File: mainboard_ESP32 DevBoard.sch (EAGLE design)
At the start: 44 parts, among them IC1 OP-AMP-2-LONG, IC3 74HC08N, K1 AQH213, X1 JST-XH-02-PIN-LONG-PAD, X2 JST-XH-04-PIN-LONG-PAD, X5 JST-XH-04-PIN-LONG-PAD, X7 1751293

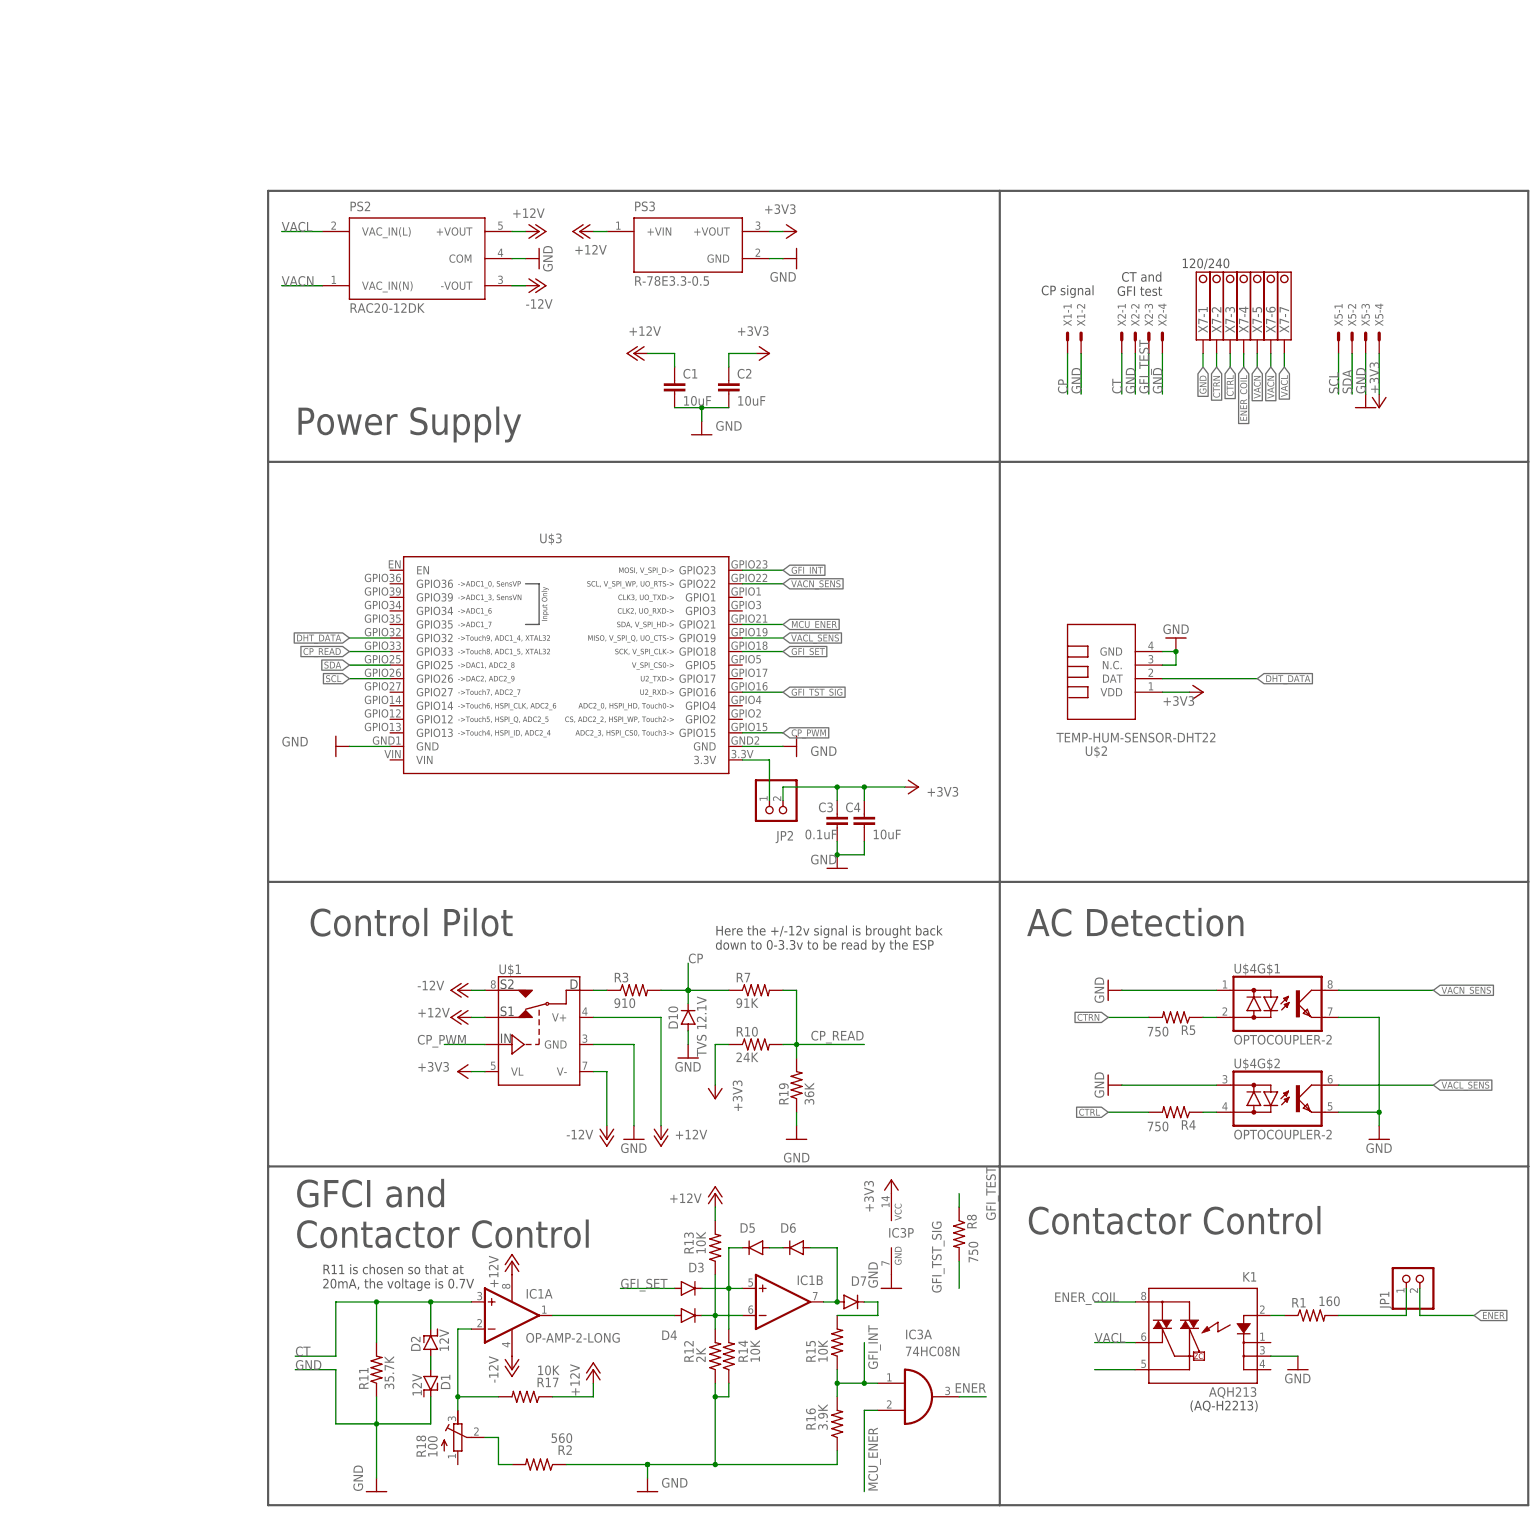
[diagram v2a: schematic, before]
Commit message: Cleaned labels
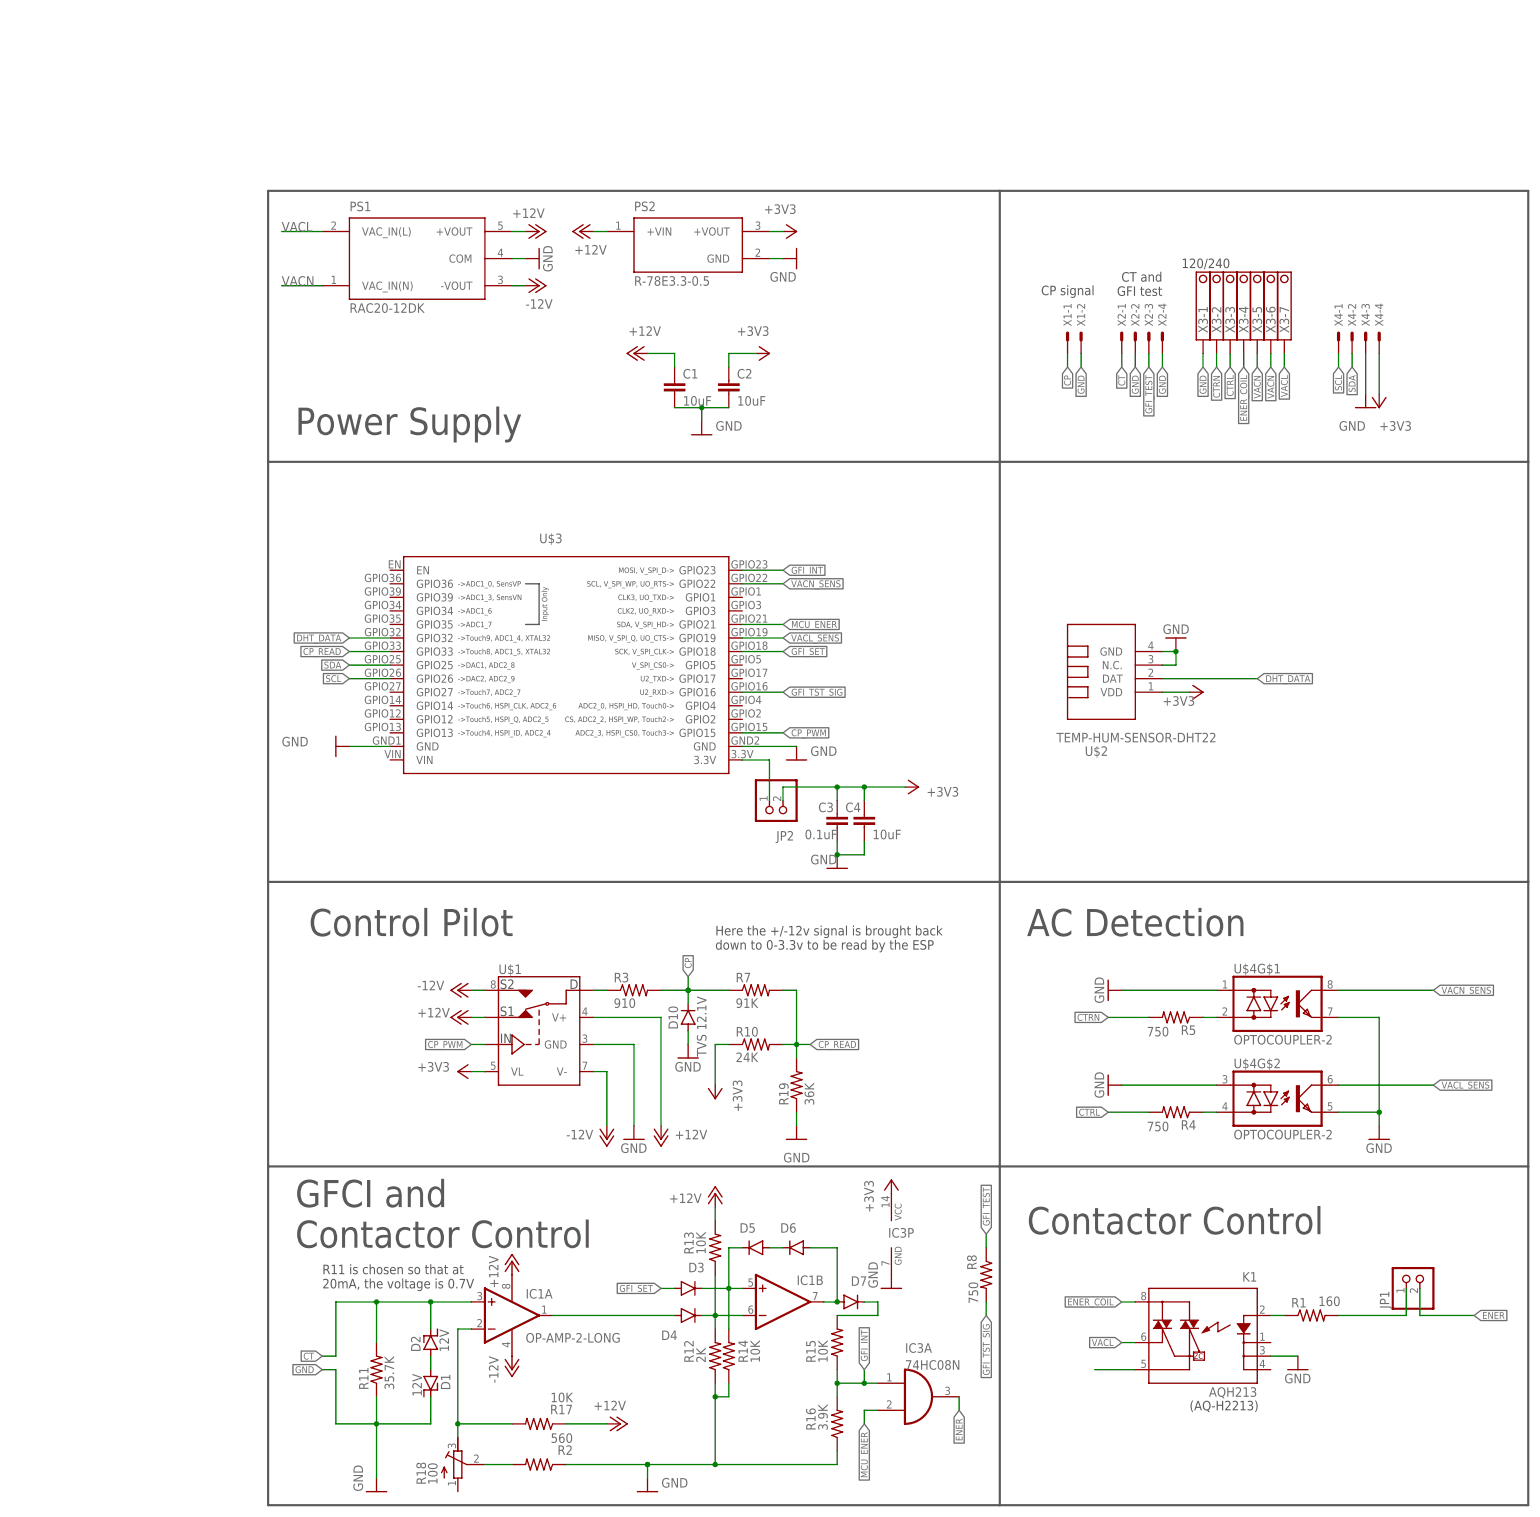
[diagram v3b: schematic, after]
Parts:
- removed PS3: R-78E3.3-0.5, R-78E3.3-0.5:R-78E3.3-0.5
- added PS1: RAC20-12DK, RAC20-12DK:RAC20-12DK
- PS2: value RAC20-12DK -> R-78E3.3-0.5; device RAC20-12DK:RAC20-12DK -> R-78E3.3-0.5:R-78E3.3-0.5
- renumbered X5 to X4, X7 to X3
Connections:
- net +12V: now also PS1.+VOUT, PS2.+VIN; no longer PS2.+VOUT, PS3.+VIN
- net +3V3: now also PS2.+VOUT; no longer PS3.+VOUT
- net -12V: now also PS1.-VOUT; no longer PS2.-VOUT
- net GND: now also PS1.COM, PS2.GND; no longer PS2.COM, PS3.GND
- net VACL: now also PS1.VAC_IN(L); no longer PS2.VAC_IN(L)
- net VACN: now also PS1.VAC_IN(N); no longer PS2.VAC_IN(N)
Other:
- moved on the sheet: R17, R18, R8

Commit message: Reworked GFCI to account for noise on the line. Swapped out AND gate for 2 mosfets. Removed mostly useless caps from PSU outputs, caps should be closer to devices
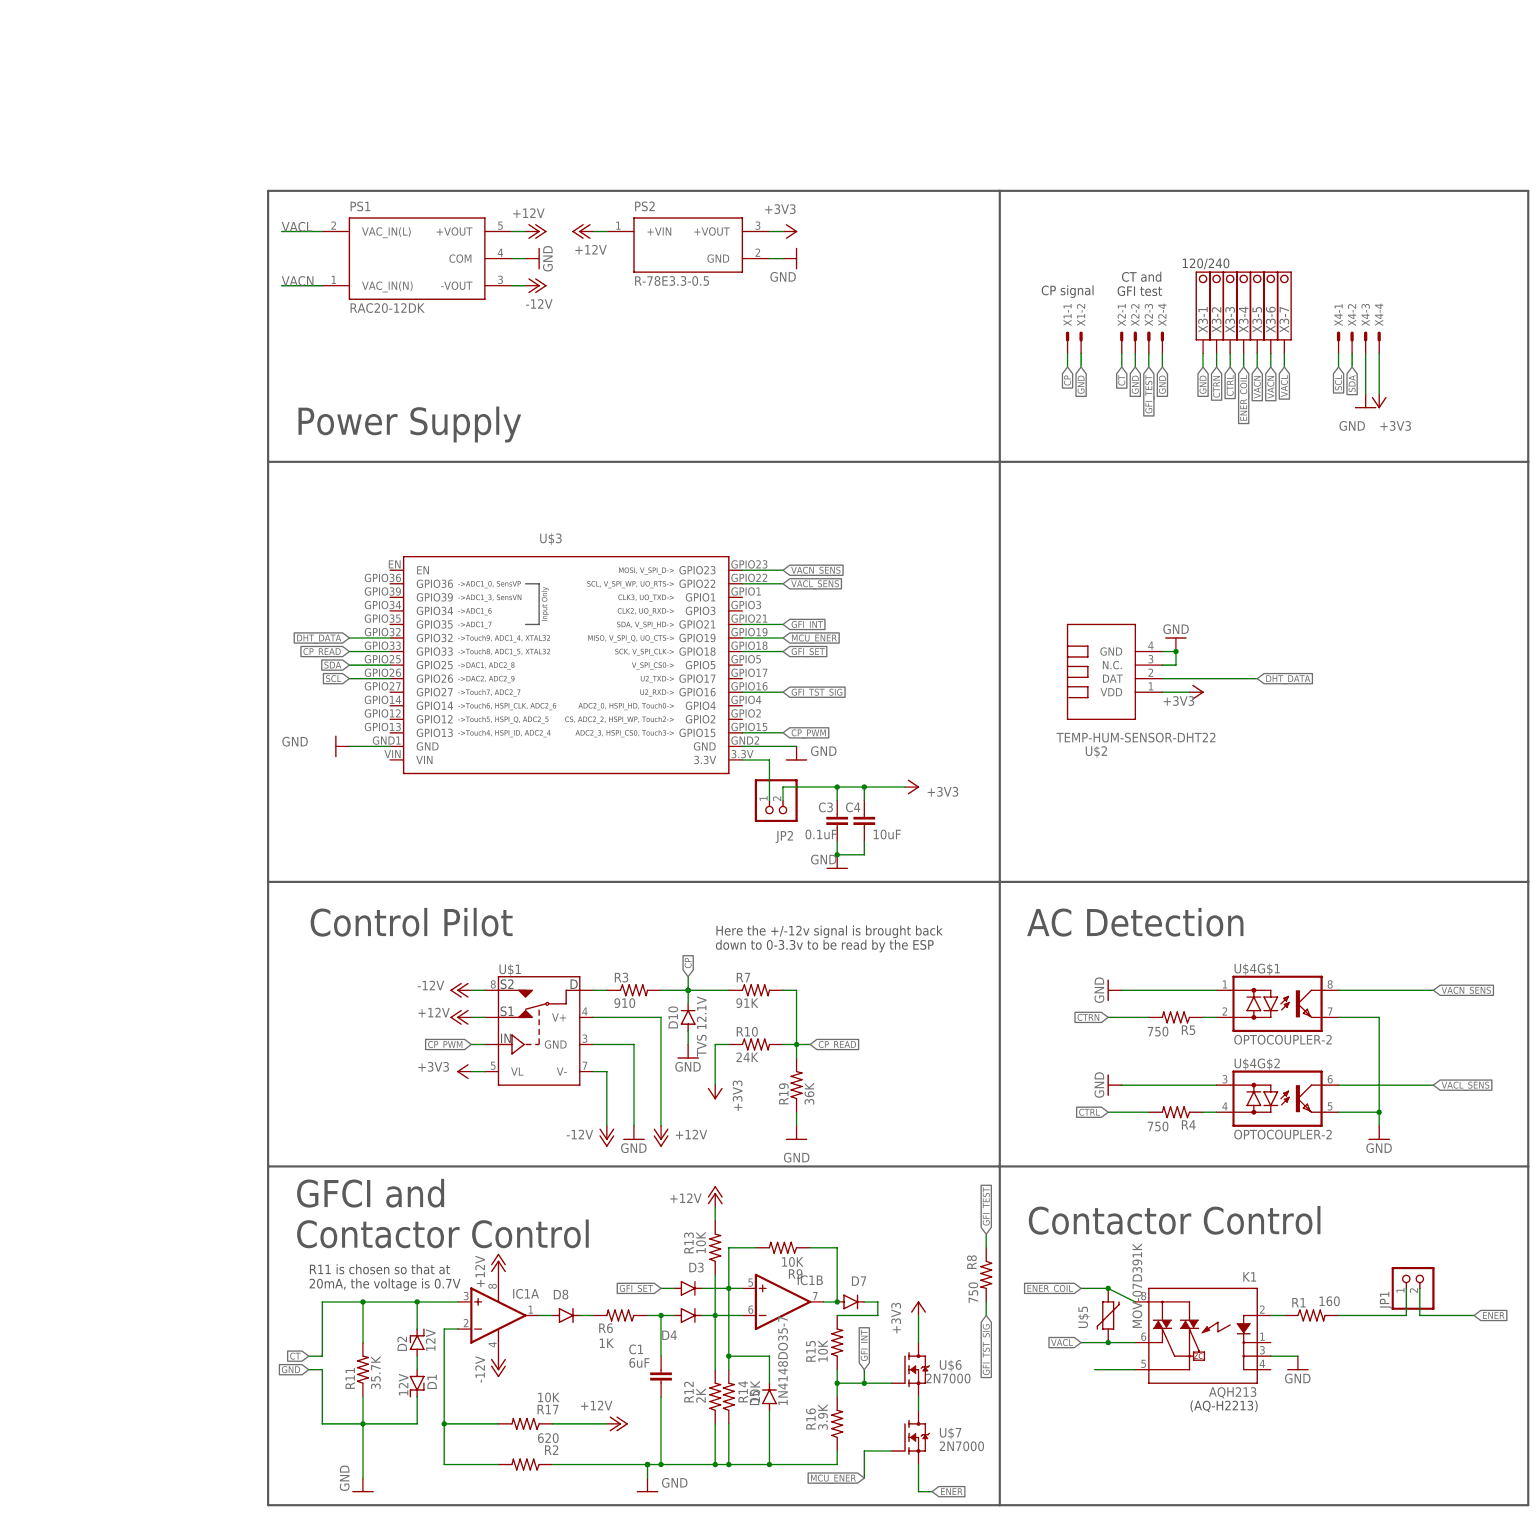
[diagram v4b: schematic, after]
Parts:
- removed C2: 10uF, rcl:C-EU025-025X050
- removed D6: 1N4148DO35-7, diode:1N4148DO35-7
- removed IC3: 74HC08N, 74xx-eu:74HC08N
- removed R18: 100, rcl:R-TRIMM3296W
- added D8: 1N4148DO35-7, diode:1N4148DO35-7
- added R6: 1K, Passive:RESISTORL
- added R9: 10K, Passive:RESISTORL
- added U$5: MOV-07D391K, EVSE:MOV-07D391K
- added U$6, U$7: 2N7000, EVSE:2N7000
- C1: value 10uF -> 6uF
- R2: value 560 -> 620
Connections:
- removed net N$12: D5.A, D6.C
- new net N$15: D8.A, IC1A.OUT
- new net N$18: U$6.S, U$7.D
- net +12V: no longer C1.1
- net +3V3: now also U$6.D; no longer C2.1, IC3P.VCC
- net ENER: now also U$7.S; no longer IC3A.O
- net ENER_COIL: now also U$5.1
- net GFI_INT: now also U$3.GPIO21, U$6.G; no longer IC3A.I0, U$3.GPIO23
- net GND: now also D5.A; no longer C2.2, IC3P.GND
- net MCU_ENER: now also U$3.GPIO19, U$7.G; no longer IC3A.I1, U$3.GPIO21
- net N$13: now also R9.2
- net N$2: now also R2.2; no longer R18.E
- net N$4: now also R9.1; no longer D6.A
- net N$6: now also D8.C, R6.2; no longer R18.S, R2.2
- net N$9: now also C1.1, R6.1; no longer IC1A.OUT
- net VACL: now also U$5.2
- net VACL_SENS: now also U$3.GPIO22; no longer U$3.GPIO19
- net VACN_SENS: now also U$3.GPIO23; no longer U$3.GPIO22
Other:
- moved on the sheet: C1, D1, D2, D5, IC1A, R11, R12, R14, R17, R2

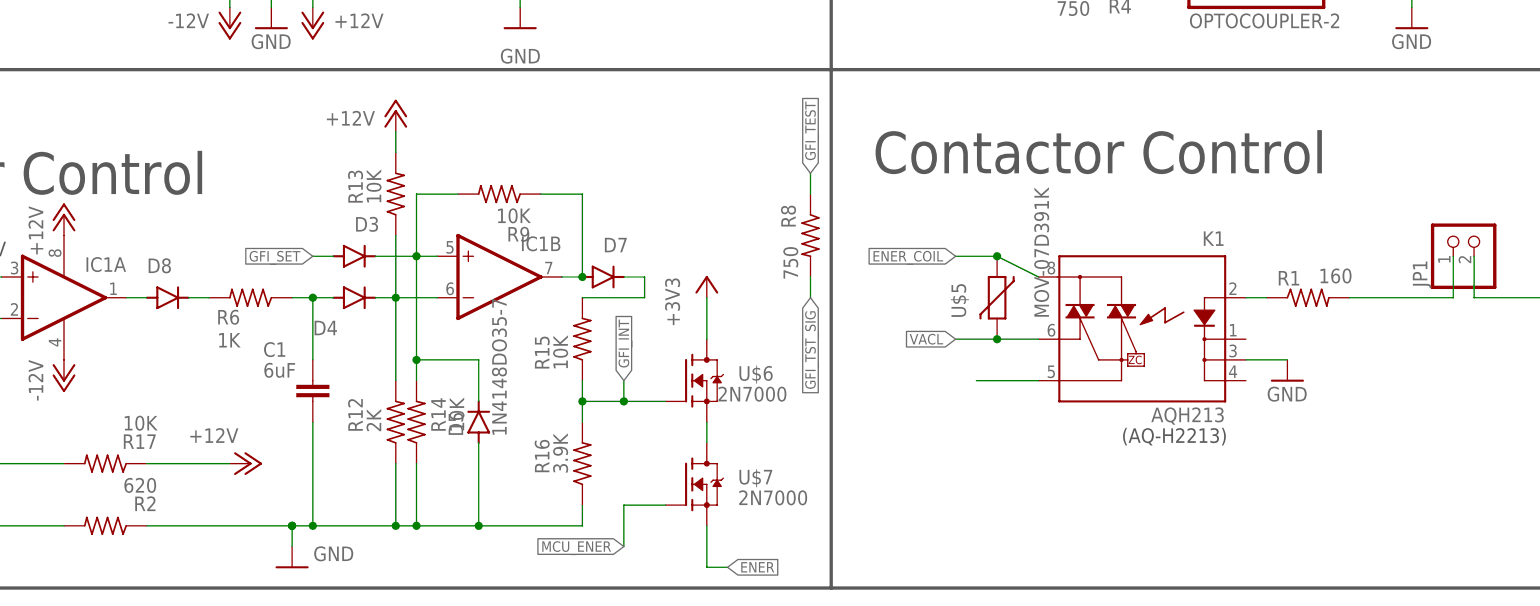
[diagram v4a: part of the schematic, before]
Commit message: Re-worked GFCI to be tolerant of transient spikes. Removed some components because of it
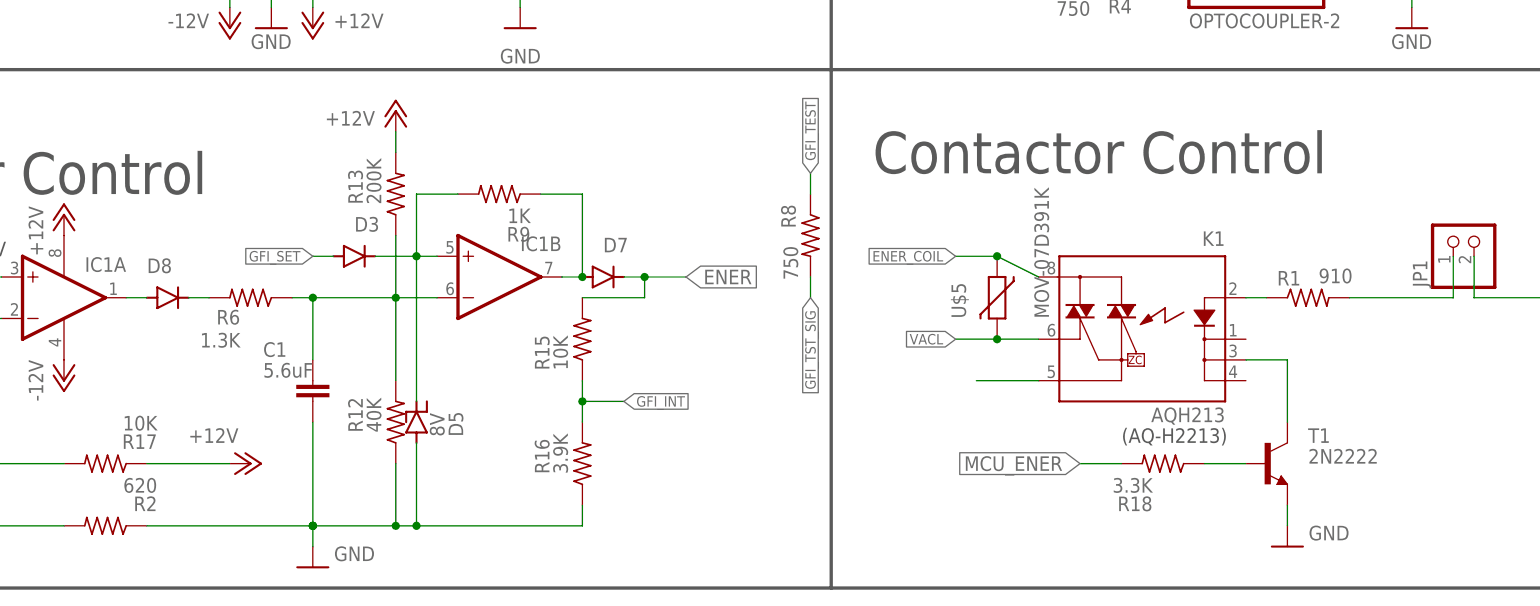
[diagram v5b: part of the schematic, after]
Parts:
- removed D4: 1N4148DO35-7, diode:1N4148DO35-7
- removed R14: 10K, Passive:RESISTORL
- removed U$6, U$7: 2N7000, EVSE:2N7000
- added R18: 3.3K, Passive:RESISTORL
- added T1: 2N2222, transistor-neu-to92:2N2222-NPN-TO92-EBC
- C1: value 6uF -> 5.6uF
- D5: value 1N4148DO35-7 -> 8V; device diode:1N4148DO35-7 -> Passive:ZENER
- R1: value 160 -> 910
- R12: value 2K -> 40K
- R13: value 10K -> 200K
- R6: value 1K -> 1.3K
- R9: value 10K -> 1K
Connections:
- removed net N$18: U$6.S, U$7.D
- removed net N$7: D7.C, R15.2
- new net N$12: R18.1, T1.B
- net +3V3: no longer U$6.D
- net ENER: now also D7.C, R15.2; no longer U$7.S
- net GFI_INT: no longer U$6.G
- net GND: now also T1.E; no longer K1.K1, R14.1
- net MCU_ENER: now also R18.2; no longer U$7.G
- net N$13: no longer R14.2
- net N$14: now also K1.K1, T1.C; no longer D4.C, IC1B.-IN, R12.2, R13.1
- net N$9: now also IC1B.-IN, R12.2, R13.1; no longer D4.A
